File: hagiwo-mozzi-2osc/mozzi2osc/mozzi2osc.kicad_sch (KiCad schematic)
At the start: 35 parts, among them J1 AudioJack2, J2 AudioJack2, J3 AudioJack2, J4 Conn_02x05_Odd_Even, SW1 SW_SPDT_MSM, U1 TL072

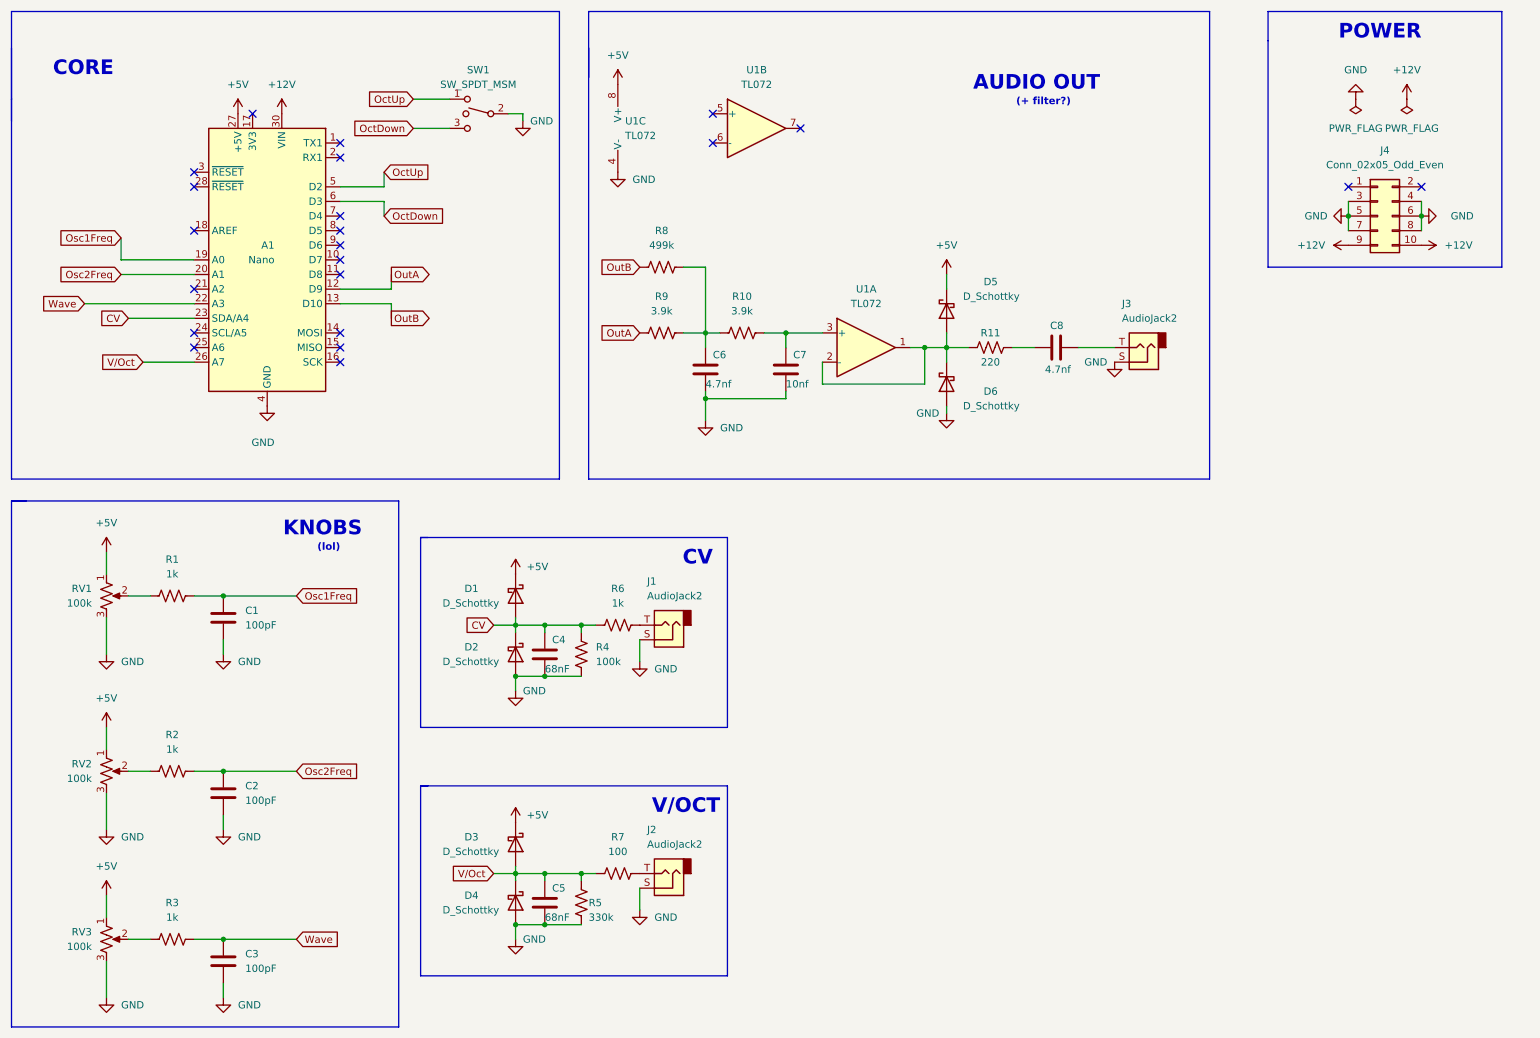
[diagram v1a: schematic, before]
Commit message: panelize 2osc
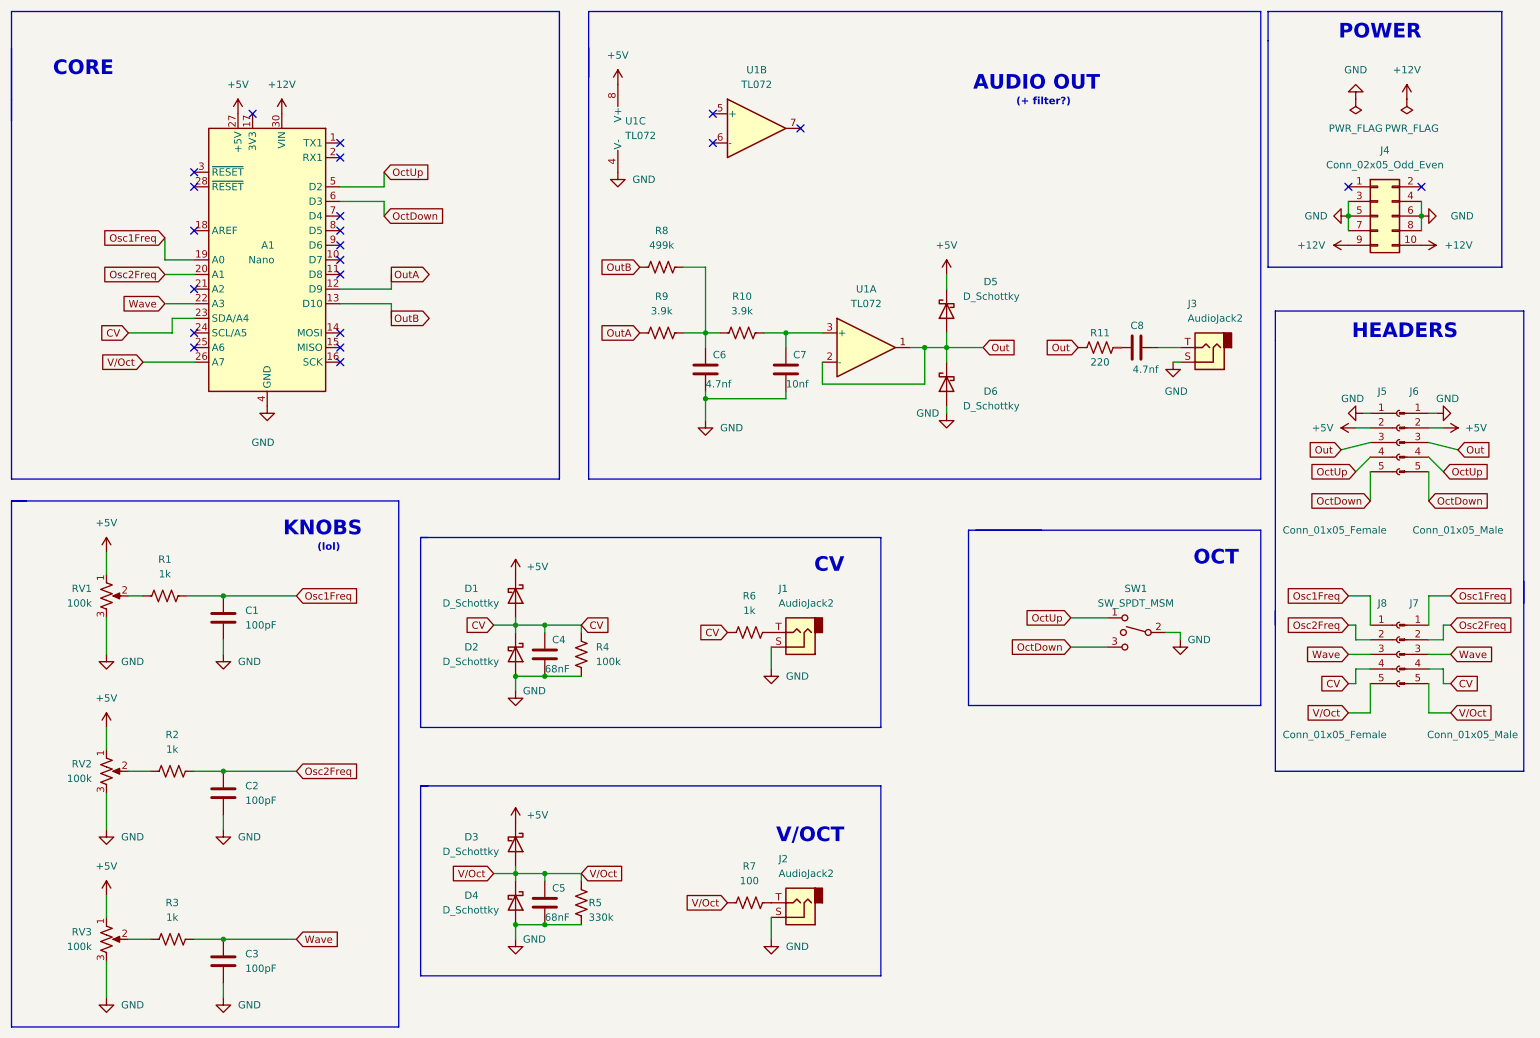
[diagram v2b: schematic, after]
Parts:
- added J5, J8: Conn_01x05_Female, Connector_PinSocket_2.54mm:PinSocket_1x05_P2.54mm_Vertical, symbol Connector:Conn_01x05_Female
- added J6, J7: Conn_01x05_Male, Connector_PinHeader_2.54mm:PinHeader_1x05_P2.54mm_Vertical, symbol Connector:Conn_01x05_Male
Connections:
- net +5V: now also J5.2 (Pin_2), J6.2 (Pin_2)
- net CV: now also J7.4 (Pin_4), J8.4 (Pin_4)
- net GND: now also J5.1 (Pin_1), J6.1 (Pin_1)
- net OctDown: now also J5.5 (Pin_5), J6.5 (Pin_5)
- net OctUp: now also J5.4 (Pin_4), J6.4 (Pin_4)
- net Osc1Freq: now also J7.1 (Pin_1), J8.1 (Pin_1)
- net Osc2Freq: now also J7.2 (Pin_2), J8.2 (Pin_2)
- net V/Oct: now also J7.5 (Pin_5), J8.5 (Pin_5)
- net Wave: now also J7.3 (Pin_3), J8.3 (Pin_3)
- net Out: now reaches D5.2 (A), D6.1 (K), R11.1, U1.1, U1.2 (-)
- net Out: now also J5.3 (Pin_3), J6.3 (Pin_3)
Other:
- note added: "HEADERS"
- note added: "OCT"
- moved on the sheet: C8, J1, J2, J3, R1, R11, R6, R7, SW1
